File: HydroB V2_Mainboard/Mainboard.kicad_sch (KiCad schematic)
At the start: 0 parts

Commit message: Mainboard schematic update
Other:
- sheet LED ports: added RXD, TXD; removed none
- sheet MCU ports: added RXD, TXD; removed none
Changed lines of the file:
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@@
 	(wire
 		(pts
-			(xy 179.07 77.47) (xy 187.96 77.47)
-		)
-		(stroke
-			(width 0)
-			(type default)
-		)
-	)
-	(wire
-		(pts
-			(xy 179.07 77.47) (xy 179.07 74.93)
+			(xy 179.07 76.2) (xy 187.96 76.2)
+		)
+		(stroke
+			(width 0)
+			(type default)
+		)
+	)
+	(wire
+		(pts
+			(xy 179.07 76.2) (xy 179.07 74.93)
+		)
+		(stroke
+			(width 0)
+			(type default)
+		)
+	)
+	(wire
+		(pts
+			(xy 179.07 91.44) (xy 168.91 91.44)
+		)
+		(stroke
+			(width 0)
+			(type default)
+		)
+	)
+	(wire
+		(pts
+			(xy 187.96 87.63) (xy 179.07 87.63)
 		)
 		(stroke
@@
 	(wire
 		(pts
+			(xy 179.07 82.55) (xy 179.07 85.09)
+		)
+		(stroke
+			(width 0)
+			(type default)
+		)
+	)
+	(wire
+		(pts
 			(xy 111.76 68.58) (xy 128.27 68.58)
 		)
@@
 	(wire
 		(pts
+			(xy 187.96 82.55) (xy 179.07 82.55)
+		)
+		(stroke
+			(width 0)
+			(type default)
+		)
+	)
+	(wire
+		(pts
 			(xy 110.49 121.92) (xy 121.92 121.92)
 		)
@@
 	(wire
 		(pts
+			(xy 179.07 87.63) (xy 179.07 91.44)
+		)
+		(stroke
+			(width 0)
+			(type default)
+		)
+	)
+	(wire
+		(pts
 			(xy 121.92 111.76) (xy 128.27 111.76)
 		)
@@
 		(pts
 			(xy 180.34 71.12) (xy 180.34 68.58)
+		)
+		(stroke
+			(width 0)
+			(type default)
+		)
+	)
+	(wire
+		(pts
+			(xy 179.07 85.09) (xy 168.91 85.09)
 		)
 		(stroke
@@
 			)
 		)
+		(pin "RXD" input
+			(at 168.91 85.09 0)
+			(effects
+				(font
+					(size 1.27 1.27)
+				)
+				(justify right)
+			)
+		)
+		(pin "TXD" input
+			(at 168.91 91.44 0)
+			(effects
+				(font
+					(size 1.27 1.27)
+				)
+				(justify right)
+			)
+		)
 		(instances
 			(project "LCD High Revolution"
@@
 	(sheet
 		(at 187.96 66.04)
-		(size 18.415 16.51)
+		(size 18.415 26.67)
 		(fields_autoplaced yes)
 		(stroke
@@
 		)
 		(property "Sheetfile" "LED.kicad_sch"
-			(at 187.96 83.1346 0)
+			(at 187.96 93.2946 0)
 			(effects
 				(font
@@
 		)
 		(pin "LED2" input
-			(at 187.96 77.47 180)
-			(effects
-				(font
+			(at 187.96 76.2 180)
+			(effects
+				(font
+					(size 1.27 1.27)
+				)
+				(justify left)
+			)
+		)
+		(pin "TXD" input
+			(at 187.96 87.63 180)
+			(effects
+				(font
+					(size 1.27 1.27)
+				)
+				(justify left)
+			)
+		)
+		(pin "RXD" input
+			(at 187.96 82.55 180)
+			(effects
+				(font

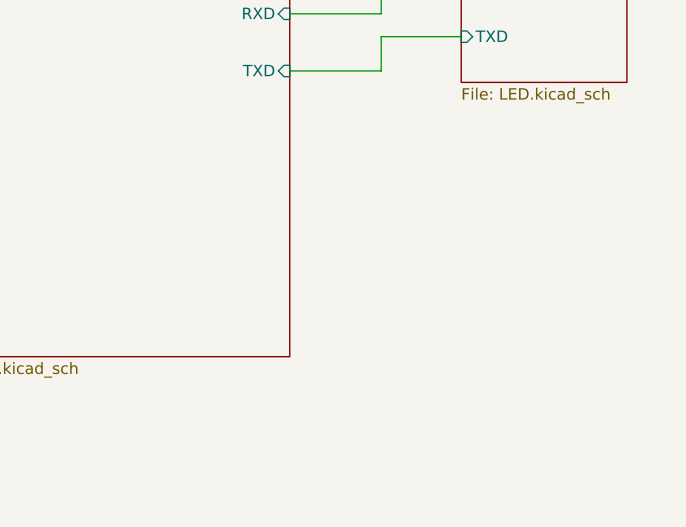
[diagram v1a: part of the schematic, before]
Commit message: main PCB board placement
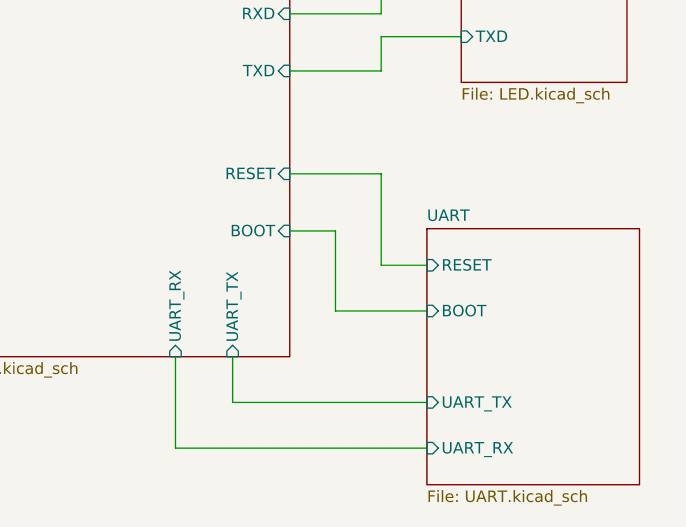
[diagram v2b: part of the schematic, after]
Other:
- added sheet UART (UART.kicad_sch)
- sheet MCU ports: added BOOT, RESET, UART_RX, UART_TX; removed none
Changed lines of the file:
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@@
+	(wire
+		(pts
+			(xy 179.07 113.03) (xy 179.07 102.87)
+		)
+		(stroke
+			(width 0)
+			(type default)
+		)
+	)
+	(wire
+		(pts
+			(xy 179.07 102.87) (xy 168.91 102.87)
+		)
+		(stroke
+			(width 0)
+			(type default)
+		)
+	)
 	(wire
 		(pts
@@
 	(wire
 		(pts
+			(xy 156.21 123.19) (xy 156.21 133.35)
+		)
+		(stroke
+			(width 0)
+			(type default)
+		)
+	)
+	(wire
+		(pts
 			(xy 179.07 82.55) (xy 179.07 85.09)
 		)
@@
 	(wire
 		(pts
+			(xy 184.15 118.11) (xy 173.99 118.11)
+		)
+		(stroke
+			(width 0)
+			(type default)
+		)
+	)
+	(wire
+		(pts
 			(xy 116.84 105.41) (xy 128.27 105.41)
 		)
@@
 	(wire
 		(pts
+			(xy 184.15 113.03) (xy 179.07 113.03)
+		)
+		(stroke
+			(width 0)
+			(type default)
+		)
+	)
+	(wire
+		(pts
 			(xy 180.34 71.12) (xy 180.34 68.58)
 		)
@@
 	(wire
 		(pts
+			(xy 156.21 133.35) (xy 184.15 133.35)
+		)
+		(stroke
+			(width 0)
+			(type default)
+		)
+	)
+	(wire
+		(pts
+			(xy 162.56 123.19) (xy 162.56 128.27)
+		)
+		(stroke
+			(width 0)
+			(type default)
+		)
+	)
+	(wire
+		(pts
 			(xy 179.07 85.09) (xy 168.91 85.09)
+		)
+		(stroke
+			(width 0)
+			(type default)
+		)
+	)
+	(wire
+		(pts
+			(xy 162.56 128.27) (xy 184.15 128.27)
+		)
+		(stroke
+			(width 0)
+			(type default)
+		)
+	)
+	(wire
+		(pts
+			(xy 173.99 118.11) (xy 173.99 109.22)
+		)
+		(stroke
+			(width 0)
+			(type default)
+		)
+	)
+	(wire
+		(pts
+			(xy 173.99 109.22) (xy 168.91 109.22)
 		)
 		(stroke
@@
 			)
 		)
+		(pin "UART_RX" input
+			(at 156.21 123.19 270)
+			(effects
+				(font
+					(size 1.27 1.27)
+				)
+				(justify left)
+			)
+		)
+		(pin "UART_TX" input
+			(at 162.56 123.19 270)
+			(effects
+				(font
+					(size 1.27 1.27)
+				)
+				(justify left)
+			)
+		)
+		(pin "BOOT" input
+			(at 168.91 109.22 0)
+			(effects
+				(font
+					(size 1.27 1.27)
+				)
+				(justify right)
+			)
+		)
+		(pin "RESET" input
+			(at 168.91 102.87 0)
+			(effects
+				(font
+					(size 1.27 1.27)
+				)
+				(justify right)
+			)
+		)
 		(instances
 			(project "LCD High Revolution"
@@
 				)
 			)
+		)
+	)
+	(sheet
+		(at 184.15 108.966)
+		(size 23.622 28.448)
+		(fields_autoplaced yes)
+		(stroke
+			(width 0.1524)
+			(type solid)
+		)
+		(fill
+			(color 255 255 194 1.0000)
+		)
+		(property "Sheetname" "UART"
+			(at 184.15 108.2544 0)
+			(effects
+				(font
+					(size 1.27 1.27)
+				)
+				(justify left bottom)
+			)
+		)
+		(property "Sheetfile" "UART.kicad_sch"
+			(at 184.15 137.9986 0)
+			(effects
+				(font
+					(size 1.27 1.27)
+				)
+				(justify left top)
+			)
+		)
+		(pin "RESET" input
+			(at 184.15 113.03 180)
+			(effects
+				(font
+					(size 1.27 1.27)
+				)
+				(justify left)
+			)
+		)
+		(pin "BOOT" input
+			(at 184.15 118.11 180)
+			(effects
+				(font
+					(size 1.27 1.27)
+				)
+				(justify left)
+			)
+		)
+		(pin "UART_TX" input
+			(at 184.15 128.27 180)
+			(effects
+				(font
+					(size 1.27 1.27)
+				)
+				(justify left)
+			)
+		)
+		(pin "UART_RX" input
+			(at 184.15 133.35 180)
+			(effects
+				(font
+					(size 1.27 1.27)
+				)
+				(justify left)
+			)
+		)
+		(instances
+			(project "LCD High Revolution"
+				(path "/7eaed49e-949c-4b32-bb59-42041e199453/cb3a589e-3872-4cde-9770-3d39d4934022"
+					(page "7")
+				)
+			)

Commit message: PCB placement and ERC
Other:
- sheet MCU ports: added none; removed D+, D-
- sheet POWER SUPPLY  ports: added none; removed D+, D-
- company: (none) -> Project review of ESP32-S3
- title: (none) -> Prak Chilifong
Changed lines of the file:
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@@
 	(generator_version "8.0")
 	(paper "A4")
+	(title_block
+		(title "Prak Chilifong")
+		(date "2024-10-06")
+		(rev "2.0")
+		(company "Project review of ESP32-S3")
+		(comment 1 "Mainboard PCB")
+	)
 	(wire
 		(pts
@@
 	(wire
 		(pts
-			(xy 116.84 105.41) (xy 128.27 105.41)
-		)
-		(stroke
-			(width 0)
-			(type default)
-		)
-	)
-	(wire
-		(pts
 			(xy 187.96 82.55) (xy 179.07 82.55)
 		)
@@
 	(wire
 		(pts
-			(xy 110.49 121.92) (xy 121.92 121.92)
-		)
-		(stroke
-			(width 0)
-			(type default)
-		)
-	)
-	(wire
-		(pts
-			(xy 116.84 116.84) (xy 116.84 105.41)
-		)
-		(stroke
-			(width 0)
-			(type default)
-		)
-	)
-	(wire
-		(pts
 			(xy 179.07 87.63) (xy 179.07 91.44)
 		)
@@
 	(wire
 		(pts
-			(xy 121.92 111.76) (xy 128.27 111.76)
-		)
-		(stroke
-			(width 0)
-			(type default)
-		)
-	)
-	(wire
-		(pts
 			(xy 111.76 78.74) (xy 128.27 78.74)
 		)
@@
 	(wire
 		(pts
-			(xy 110.49 116.84) (xy 116.84 116.84)
-		)
-		(stroke
-			(width 0)
-			(type default)
-		)
-	)
-	(wire
-		(pts
 			(xy 180.34 71.12) (xy 187.96 71.12)
 		)
@@
 		(pts
 			(xy 179.07 74.93) (xy 168.91 74.93)
-		)
-		(stroke
-			(width 0)
-			(type default)
-		)
-	)
-	(wire
-		(pts
-			(xy 121.92 121.92) (xy 121.92 111.76)
 		)
 		(stroke
@@
 			)
 		)
-		(pin "D-" input
-			(at 128.27 111.76 180)
-			(effects
-				(font
-					(size 1.27 1.27)
-				)
-				(justify left)
-			)
-		)
-		(pin "D+" input
-			(at 128.27 105.41 180)
-			(effects
-				(font
-					(size 1.27 1.27)
-				)
-				(justify left)
-			)
-		)
 		(pin "EN_RS485" input
 			(at 128.27 68.58 180)
@@
 			(project "LCD High Revolution"
 				(path "/7eaed49e-949c-4b32-bb59-42041e199453/cb3a589e-3872-4cde-9770-3d39d4934022"
-					(page "8")
+					(page "6")
 				)
 			)
@@
 			(project "LCD High Revolution"
 				(path "/7eaed49e-949c-4b32-bb59-42041e199453/cb3a589e-3872-4cde-9770-3d39d4934022"
-					(page "7")
+					(page "5")
 				)
 			)
@@
 			)
 		)
-		(pin "D-" input
-			(at 110.49 121.92 0)
-			(effects
-				(font
-					(size 1.27 1.27)
-				)
-				(justify right)
-			)
-		)
-		(pin "D+" input
-			(at 110.49 116.84 0)
-			(effects
-				(font
-					(size 1.27 1.27)
-				)
-				(justify right)
-			)
-		)
 		(instances
 			(project "LCD High Revolution"
 				(path "/7eaed49e-949c-4b32-bb59-42041e199453/cb3a589e-3872-4cde-9770-3d39d4934022"
-					(page "8")
+					(page "7")
 				)
 			)
@@
 			(project "LCD High Revolution"
 				(path "/7eaed49e-949c-4b32-bb59-42041e199453/cb3a589e-3872-4cde-9770-3d39d4934022"
-					(page "6")
-				)
-			)
+					(page "4")
+				)
+			)
